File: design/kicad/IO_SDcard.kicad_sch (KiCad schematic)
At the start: 41 parts, among them J1 Midi_In, J11 Line_In, J3 Midi_Out, SW1 SW_DPDT_x2, U1 MCP6002-xSN, U2 H11L1S(TA), U9 MCP6002-xSN

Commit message: routes PCB all except PWR
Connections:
- net GND: now also USBC1.A1 (GND)
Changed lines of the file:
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@@
+	(wire
+		(pts
+			(xy 247.65 66.04) (xy 250.19 66.04)
+		)
+		(stroke
+			(width 0)
+			(type default)
+		)
+	)
 	(wire
 		(pts
@@
 		(pts
 			(xy 158.75 40.64) (xy 158.75 44.45)
+		)
+		(stroke
+			(width 0)
+			(type default)
+		)
+	)
+	(wire
+		(pts
+			(xy 250.19 66.04) (xy 250.19 67.31)
 		)
 		(stroke
@@
 					(unit 1)
 				)
+			)
+		)
+	)
+	(symbol
+		(lib_id "power:GND")
+		(at 250.19 67.31 0)
+		(unit 1)
+		(exclude_from_sim no)
+		(in_bom yes)
+		(on_board yes)
+		(dnp no)
+		(fields_autoplaced yes)
+		(property "Reference" "#PWR015"
+			(at 250.19 73.66 0)
+			(effects
+				(font
+					(size 1.27 1.27)
+				)
+				(hide yes)
+			)
+		)
+		(property "Value" "GND"
+			(at 250.19 72.39 0)
+			(effects
+				(font
+					(size 1.27 1.27)
+				)
+			)
+		)
+		(property "Footprint" ""
+			(at 250.19 67.31 0)
+			(effects
+				(font
+					(size 1.27 1.27)
+				)
+				(hide yes)
+			)
+		)
+		(property "Datasheet" ""
+			(at 250.19 67.31 0)
+			(effects
+				(font
+					(size 1.27 1.27)
+				)
+				(hide yes)
+			)
+		)
+		(property "Description" "Power symbol creates a global label with name \"GND\" , ground"
+			(at 250.19 67.31 0)
+			(effects
+				(font
+					(size 1.27 1.27)
+				)
+				(hide yes)
+			)
+		)
+		(pin "1"
+		)
+		(instances
+			(project "soundpad"
+				(path "/e7f7d9eb-c978-4dc1-9b91-2f2a4525cbe7/1fe70b28-8b31-4106-8d94-8f01409bdfba"
+					(reference "#PWR015")
+					(unit 1)
+				)

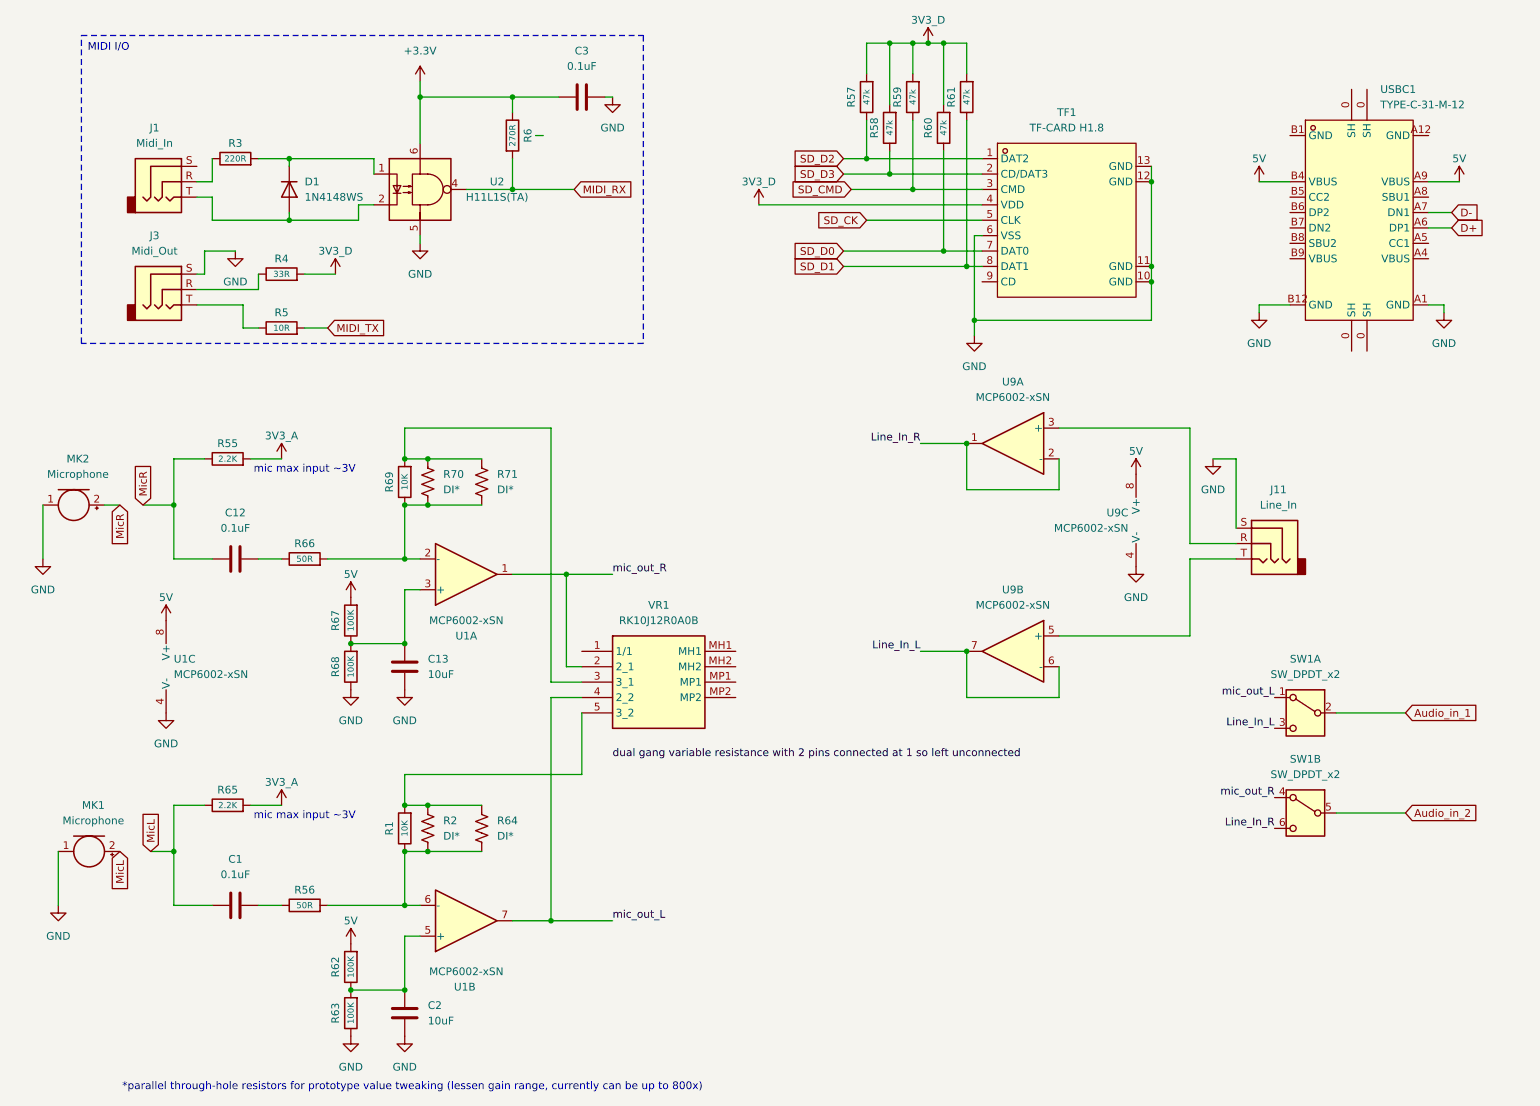
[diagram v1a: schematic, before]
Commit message: PCB all routed, Moves top components to top file
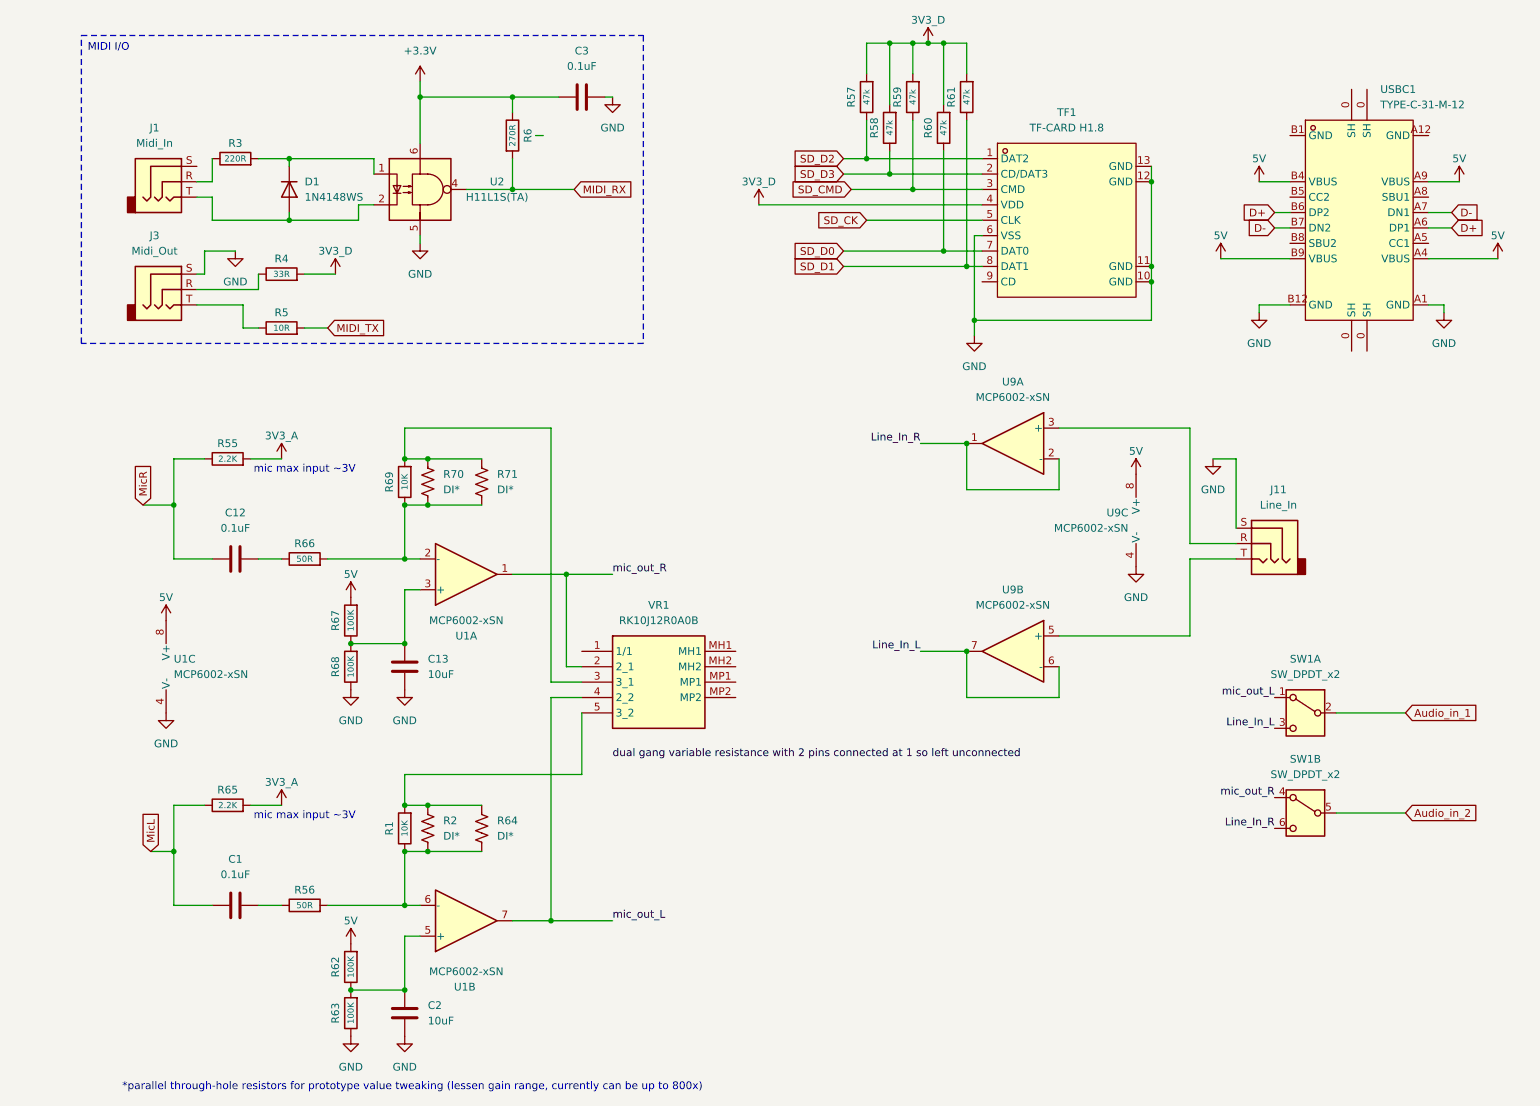
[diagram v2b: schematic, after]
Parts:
- removed MK1, MK2: Microphone, soundpad_library:AOM-5024L-HD-R, symbol Device:Microphone
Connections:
- net 5V: now also USBC1.A4 (VBUS), USBC1.B9 (VBUS)
- net D+: now also USBC1.B6 (DP2)
- net D-: now also USBC1.B7 (DN2)

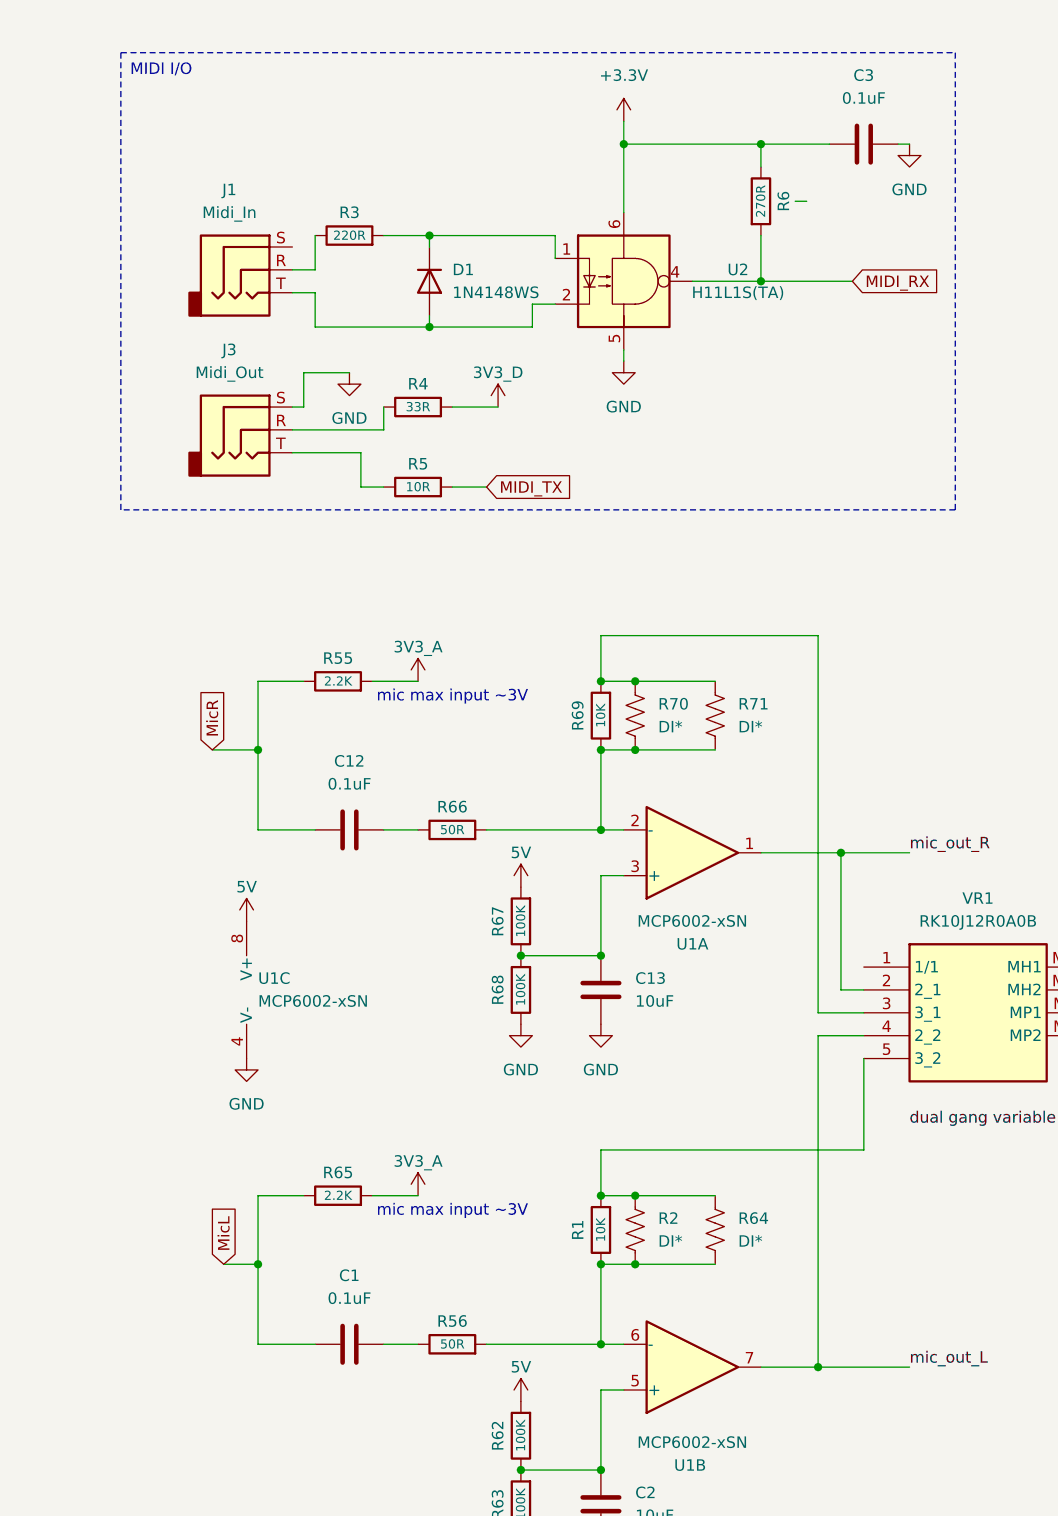
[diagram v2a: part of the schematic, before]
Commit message: shortens SD data lines
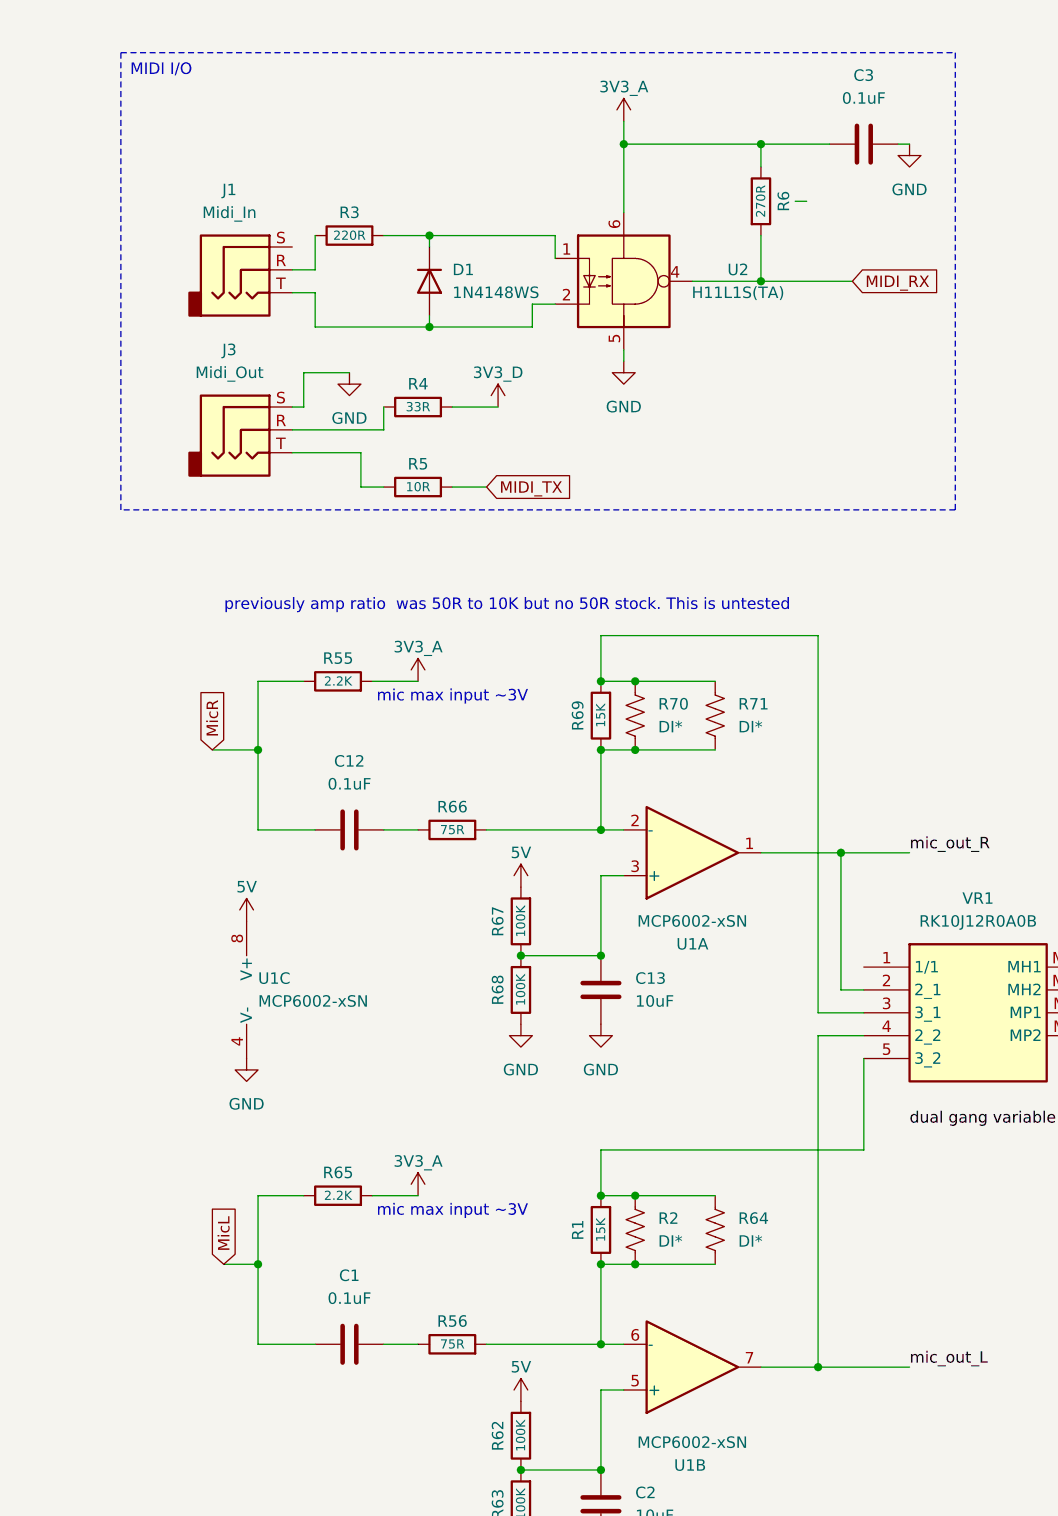
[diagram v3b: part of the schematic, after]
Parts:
- R1, R69: value 10K -> 15K
- R56, R66: value 50R -> 75R
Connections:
- net +3.3V is gone; now on net 3V3_A: C3.2, R6.1, U2.6
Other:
- note added: "previously amp ratio was 50R to 10K but no 50R stock. This is untested"
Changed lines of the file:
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@@
 		)
 	)
+	(text "previously amp ratio  was 50R to 10K but no 50R stock. This is untested"
+		(exclude_from_sim no)
+		(at 68.326 83.058 0)
+		(effects
+			(font
+				(size 1.27 1.27)
+			)
+		)
+	)
 	(text "mic max input ~3V"
 		(exclude_from_sim no)
@@
 			)
 		)
-		(property "Value" "50R"
+		(property "Value" "75R"
 			(at 62.23 165.1 90)
 			(effects
@@
 	)
 	(symbol
-		(lib_id "power:+3.3V")
-		(at 81.28 29.21 0)
-		(unit 1)
-		(exclude_from_sim no)
-		(in_bom yes)
-		(on_board yes)
-		(dnp no)
-		(fields_autoplaced yes)
-		(property "Reference" "#PWR03"
-			(at 81.28 33.02 0)
-			(effects
-				(font
-					(size 1.27 1.27)
-				)
-				(hide yes)
-			)
-		)
-		(property "Value" "+3.3V"
-			(at 81.28 24.13 0)
-			(effects
-				(font
-					(size 1.27 1.27)
-				)
-			)
-		)
-		(property "Footprint" ""
-			(at 81.28 29.21 0)
-			(effects
-				(font
-					(size 1.27 1.27)
-				)
-				(hide yes)
-			)
-		)
-		(property "Datasheet" ""
-			(at 81.28 29.21 0)
-			(effects
-				(font
-					(size 1.27 1.27)
-				)
-				(hide yes)
-			)
-		)
-		(property "Description" ""
-			(at 81.28 29.21 0)
-			(effects
-				(font
-					(size 1.27 1.27)
-				)
-				(hide yes)
-			)
-		)
-		(pin "1"
-		)
-		(instances
-			(project "soundpad"
-				(path "/e7f7d9eb-c978-4dc1-9b91-2f2a4525cbe7/1fe70b28-8b31-4106-8d94-8f01409bdfba"
-					(reference "#PWR03")
-					(unit 1)
-				)
-			)
-		)
-	)
-	(symbol
 		(lib_id "Connector_Audio:AudioJack3")
 		(at 39.37 45.72 0)
@@
 			)
 		)
-		(property "Value" "10K"
+		(property "Value" "15K"
 			(at 78.74 95.25 90)
 			(effects
@@
 	)
 	(symbol
+		(lib_id "daisy_seed:3V3_A")
+		(at 81.28 29.21 0)
+		(unit 1)
+		(exclude_from_sim no)
+		(in_bom yes)
+		(on_board yes)
+		(dnp no)
+		(fields_autoplaced yes)
+		(property "Reference" "#PWR03"
+			(at 81.28 33.02 0)
+			(effects
+				(font
+					(size 1.27 1.27)
+				)
+				(hide yes)
+			)
+		)
+		(property "Value" "3V3_A"
+			(at 81.28 25.4 0)
+			(effects
+				(font
+					(size 1.27 1.27)
+				)
+			)
+		)
+		(property "Footprint" ""
+			(at 81.28 29.21 0)
+			(effects
+				(font
+					(size 1.27 1.27)
+				)
+				(hide yes)
+			)
+		)
+		(property "Datasheet" ""
+			(at 81.28 29.21 0)
+			(effects
+				(font
+					(size 1.27 1.27)
+				)
+				(hide yes)
+			)
+		)
+		(property "Description" "Power symbol creates a global label with name \"3V3_A\" (I hope)"
+			(at 81.28 29.21 0)
+			(effects
+				(font
+					(size 1.27 1.27)
+				)
+				(hide yes)
+			)
+		)
+		(pin "1"
+		)
+		(instances
+			(project "soundpad_economy"
+				(path "/e7f7d9eb-c978-4dc1-9b91-2f2a4525cbe7/1fe70b28-8b31-4106-8d94-8f01409bdfba"
+					(reference "#PWR03")
+					(unit 1)
+				)
+			)
+		)
+	)
+	(symbol
 		(lib_id "Device:R")
 		(at 69.85 125.73 180)
@@
 			)
 		)
-		(property "Value" "50R"
+		(property "Value" "75R"
 			(at 62.23 107.95 90)
 			(effects
@@
 			)
 		)
-		(property "Value" "10K"
+		(property "Value" "15K"
 			(at 78.74 152.4 90)
 			(effects
@@
 					(reference "R6")
 					(unit 1)
+				)
+				(path "/e7f7d9eb-c978-4dc1-9b91-2f2a4525cbe7/9194bf31-8079-4b2f-befe-901822c457d4"
+					(reference "R6")
+					(unit 1)

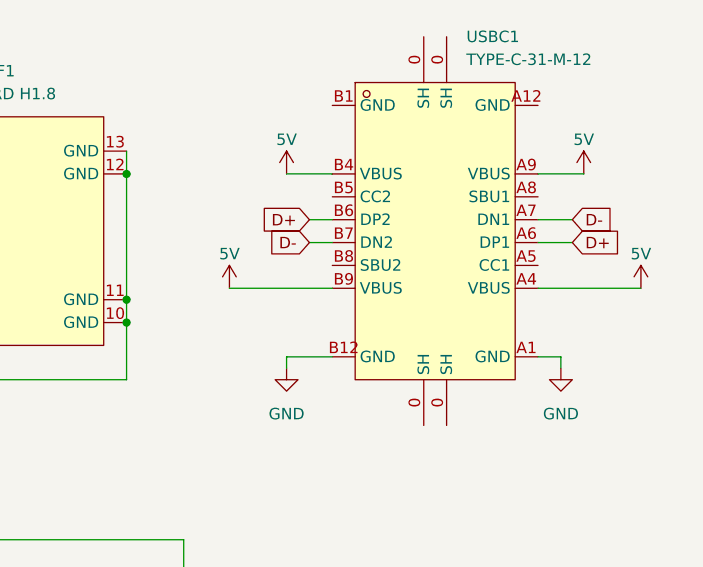
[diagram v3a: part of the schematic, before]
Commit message: pcb rules fixes, reroute suggestions
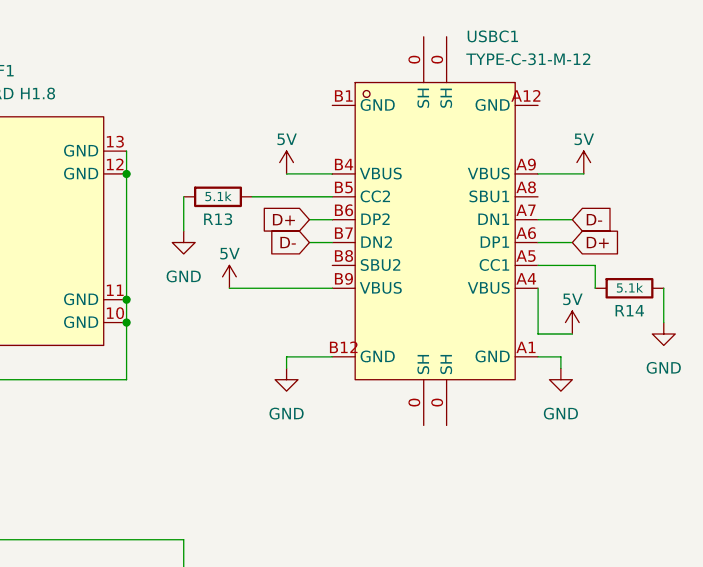
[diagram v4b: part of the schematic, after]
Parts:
- added R13, R14: 5.1k, Resistor_SMD:R_0603_1608Metric, symbol Device:R
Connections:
- net GND: now also R13.2, R14.1
- net at USBC1.A5 (CC1): now also R14.2
- net at USBC1.B5 (CC2): now also R13.1
